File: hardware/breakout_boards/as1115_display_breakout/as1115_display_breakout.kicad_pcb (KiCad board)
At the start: 2 copper layers, 44.4 x 21.6 mm, 5 parts, among them J1 7SEG_DEBUG, U1 AS1115, U2 LTC-4727JS

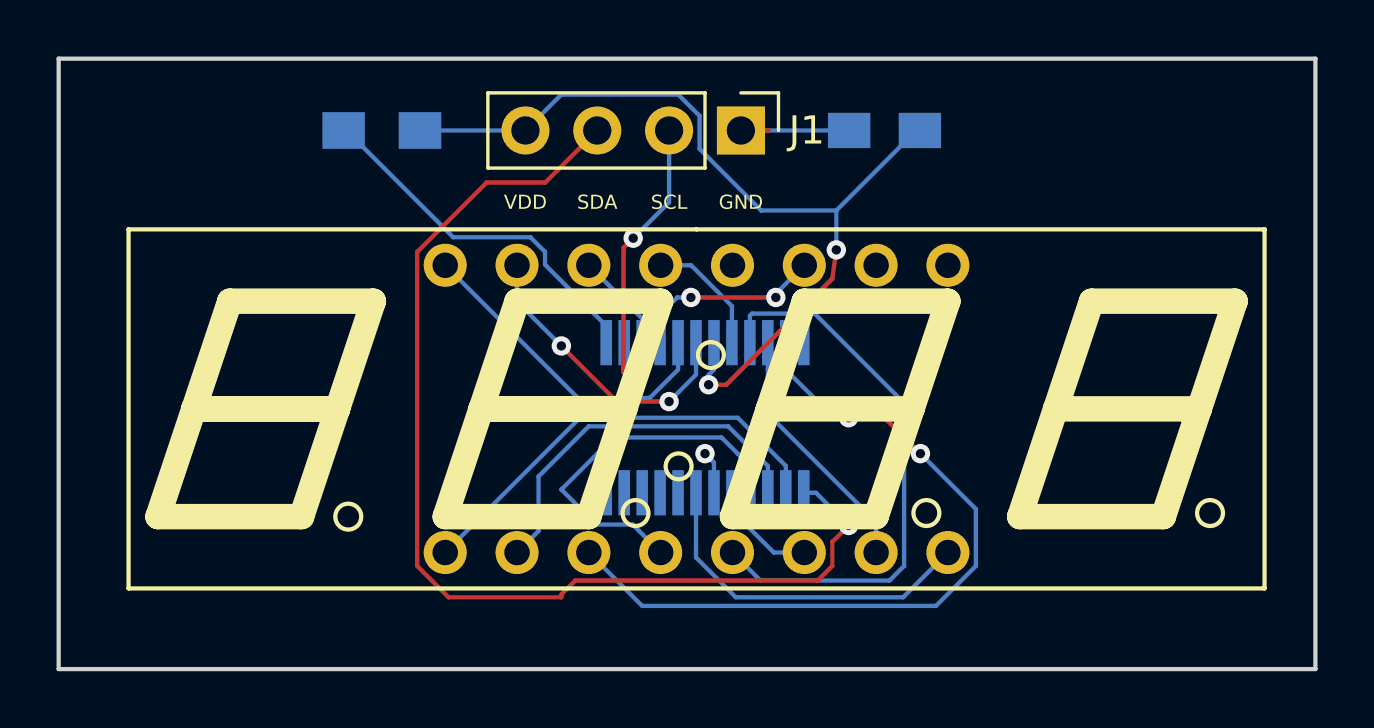
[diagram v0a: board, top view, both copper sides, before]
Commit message: Add pullup resistors, logo and text
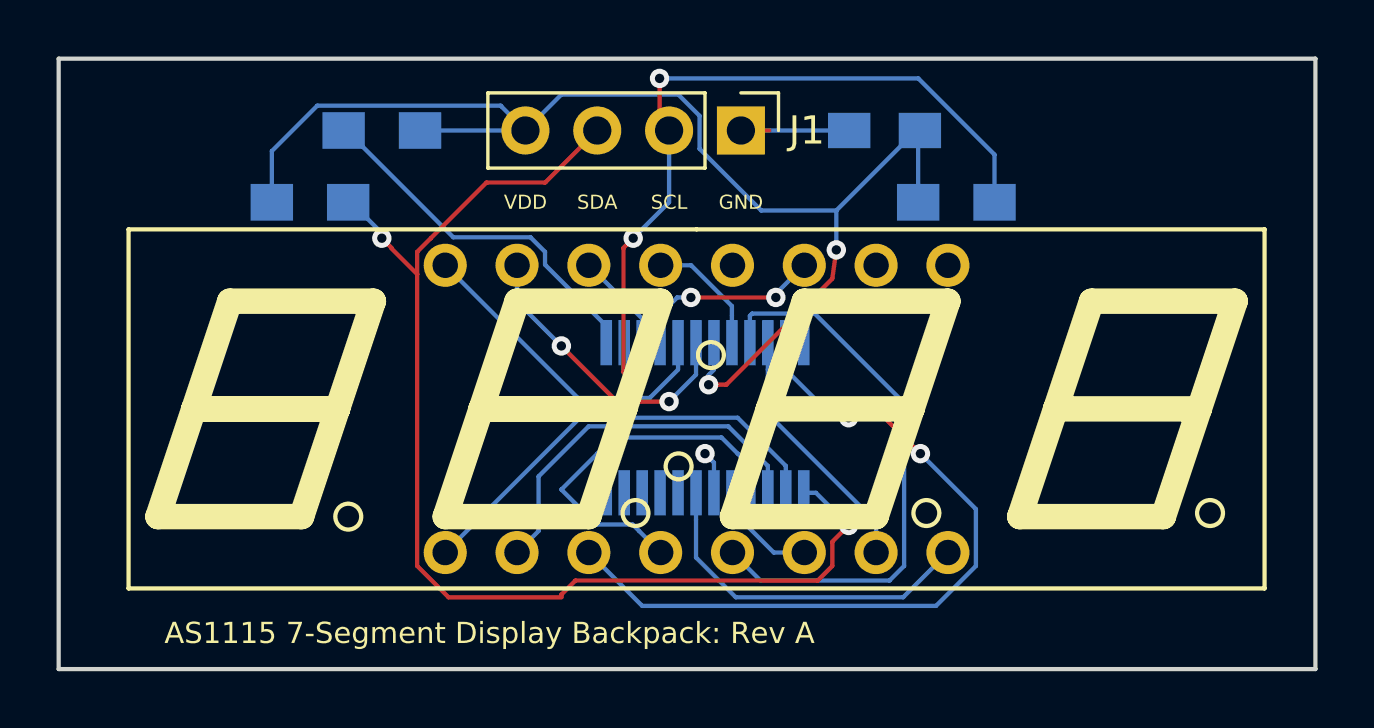
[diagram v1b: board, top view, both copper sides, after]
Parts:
- added R2: 10K, Resistors_SMD:R_0805_HandSoldering, B.Cu at (43.2, 27.9)
- added R3: 10K, Resistors_SMD:R_0805_HandSoldering, B.Cu at (66.0, 27.9)
- added REF***: OSHW-Symbol_6.7x6mm_SilkScreen, Symbols:OSHW-Symbol_6.7x6mm_SilkScreen, B.Cu at (43.2, 35.6)
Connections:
- net /7SEG_SCL renamed Net-(J1-Pad2)
- net /7SEG_SDA renamed Net-(J1-Pad3)
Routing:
- net Net-(J1-Pad2): track 11.2 -> 27.9 mm, vias 2 -> 3
- net +3V3: track 31.8 -> 46.2 mm
- net Net-(J1-Pad3): track 38.7 -> 42.3 mm, vias 1 -> 2
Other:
- board text added: "AS1115 7-Segment Display Backpack: Rev A"
